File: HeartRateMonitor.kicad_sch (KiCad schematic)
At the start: 62 parts, among them J1 USB_C_Receptacle_USB2.0, J2 SWD, J3 Conn_01x08_Pin, U1 CH340E, U10 TLV9301, U2 TLV9301, U3 TLV62130, U4 STM32G030F6Px, U5 TPS60403, U6 TLV9301, U7 TLV9301, U8 TLV9301, U9 AD5272BCP

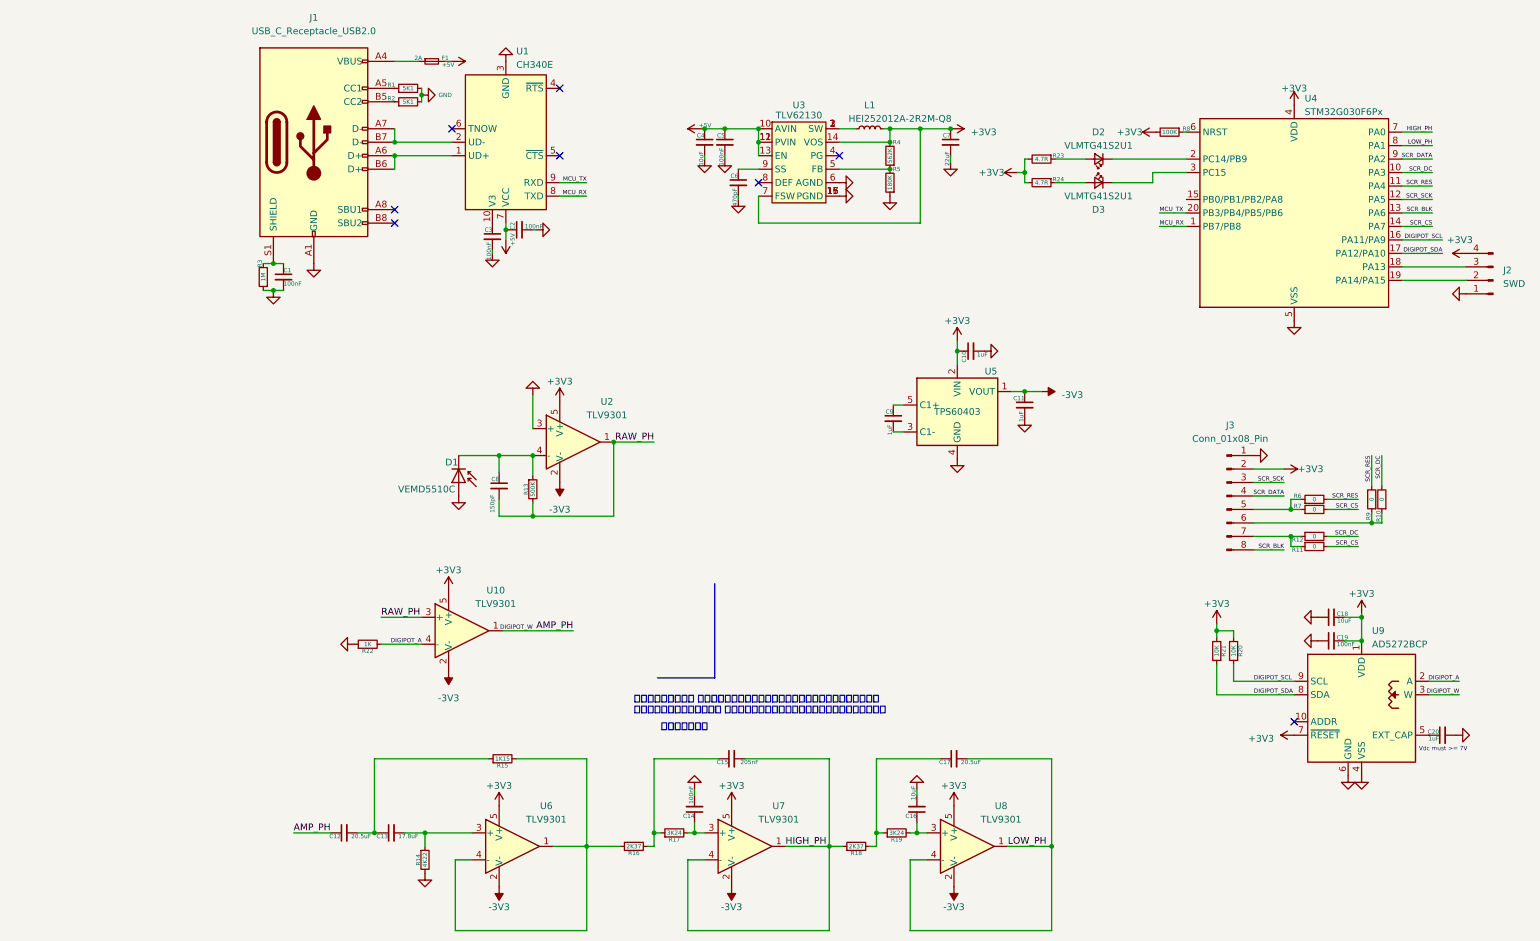
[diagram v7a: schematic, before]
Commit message: slightly modified filter and generated fabrication output
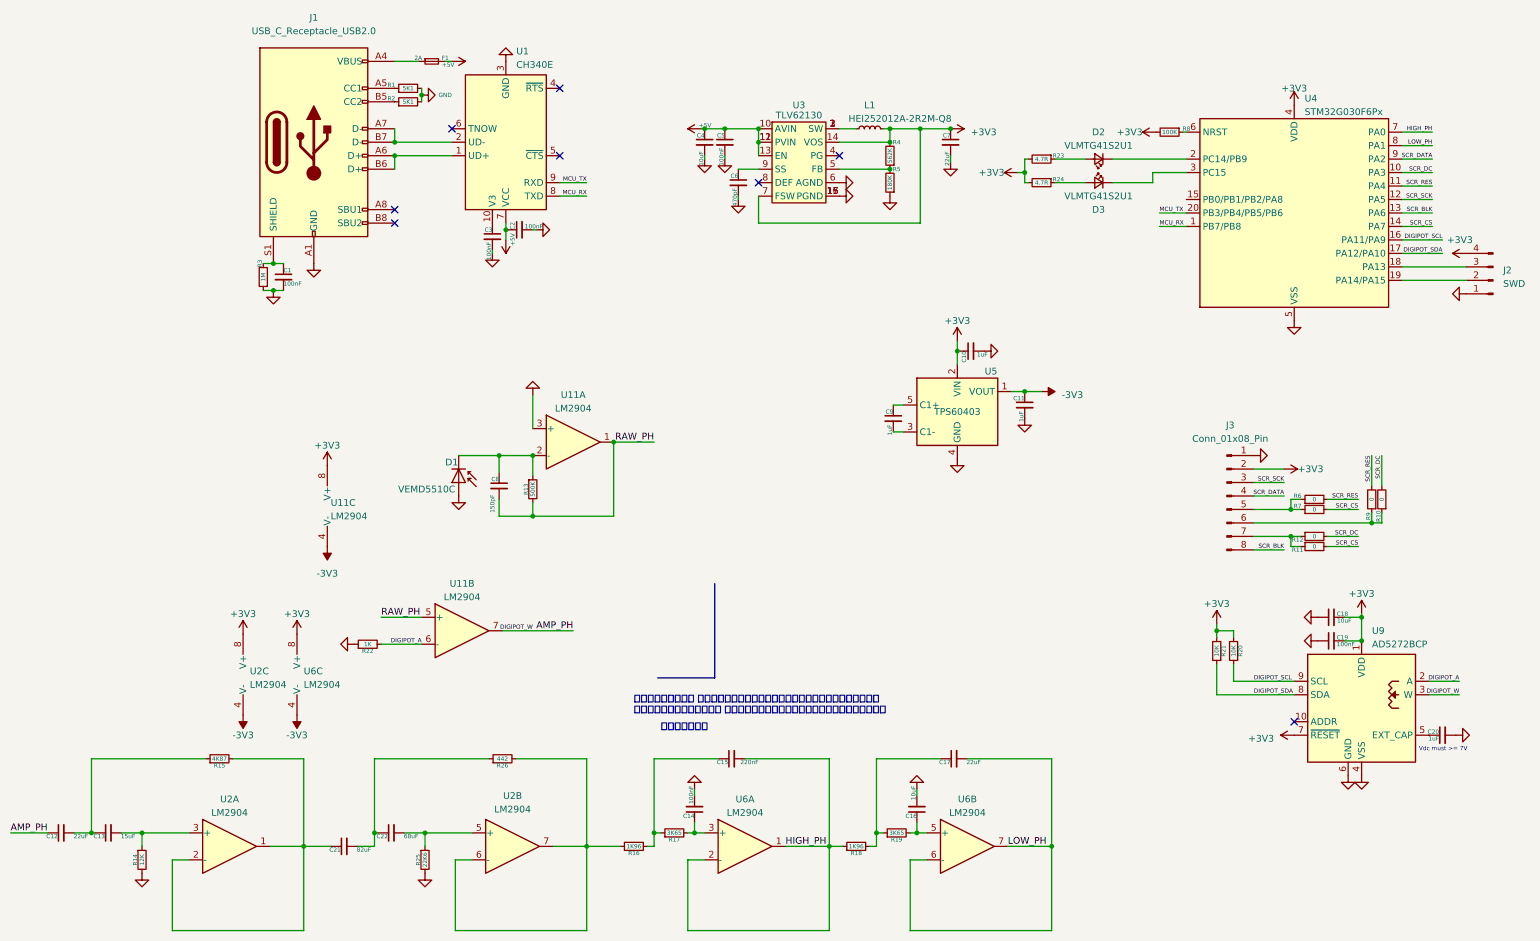
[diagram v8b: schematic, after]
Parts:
- removed U10, U2, U6, U7, U8: TLV9301, Package_TO_SOT_SMD:SOT-23-5, symbol Amplifier_Operational:LMH6702MF
- added C21: 82uF, Capacitor_SMD:C_0603_1608Metric, symbol Device:C_Small
- added C22: 68uF, Capacitor_SMD:C_0603_1608Metric, symbol Device:C_Small
- added R25: 22K6, Resistor_SMD:R_0603_1608Metric, symbol Device:R_Small
- added R26: 442, Resistor_SMD:R_0603_1608Metric, symbol Device:R_Small
- added U11, U2, U6: LM2904, symbol Amplifier_Operational:LM2904
- C12: value 20.5uF -> 22uF; footprint Capacitor_SMD:C_0603_1608Metric -> Capacitor_SMD:C_0805_2012Metric
- C13: value 17.8uF -> 15uF; footprint Capacitor_SMD:C_0603_1608Metric -> Capacitor_SMD:C_0402_1005Metric
- C15: value 205nF -> 220nF
- C17: value 20.5uF -> 22uF
- R14: value 4K22 -> 12K
- R15: value 1K15 -> 4K87
- R16, R18: value 2K37 -> 1K96
- R17, R19: value 3K24 -> 3K65
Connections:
- net +3V3: now also U11.8 (V+), U2.8 (V+), U6.8 (V+)
- net -3V3: now also U11.4 (V-), U2.4 (V-), U6.4 (V-)
- net AMP_PH: now also U11.7
- net DIGIPOT_A: now also U11.6 (-)
- net GND: now also R25.2, U11.3 (+)
- net HIGH_PH: now also U6.1, U6.2 (-)
- net LOW_PH: now also U6.6 (-), U6.7
- net RAW_PH: now also U11.1, U11.5 (+)
- net at C16.1, R19.2: now also U6.5 (+)
- net at C14.1, R17.2: now also U6.3 (+)
- net at R16.1: now also R26.2, U2.6 (-), U2.7; no longer R15.2
- net at C13.2, R14.1: now also U2.3 (+)
- net at C8.1, D1.1 (K), R13.1: now also U11.2 (-)
- new net: C21.2, C22.1, R26.1
- new net: C22.2, R25.1, U2.5 (+)
- new net: C21.1, R15.2, U2.1, U2.2 (-)
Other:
- moved on the sheet: C12, C13, R14, R15
